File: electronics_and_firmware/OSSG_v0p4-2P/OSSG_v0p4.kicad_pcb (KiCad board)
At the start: 4 copper layers, 85 x 9 mm, 72 parts, among them J1 Conn_01x05_Male, J2 Ext RGB, J3 USB_B_Micro, J4 Touch, Q1 2SC4617R BR, Q2 2SC4617R BR, Q3 PMZ290UNE2YL, Q4 EMF20B02V, SW1 SW_SPST, SW2 Power, U1 MP23DB01HPTR, U2 ESP32-PICO-D4, U3 CH9102F, U4 XC61CC3002MR, U5 AP5054HTC, U6 MAX17048, U7 NCP167BMX330TBG, U8 SY7088

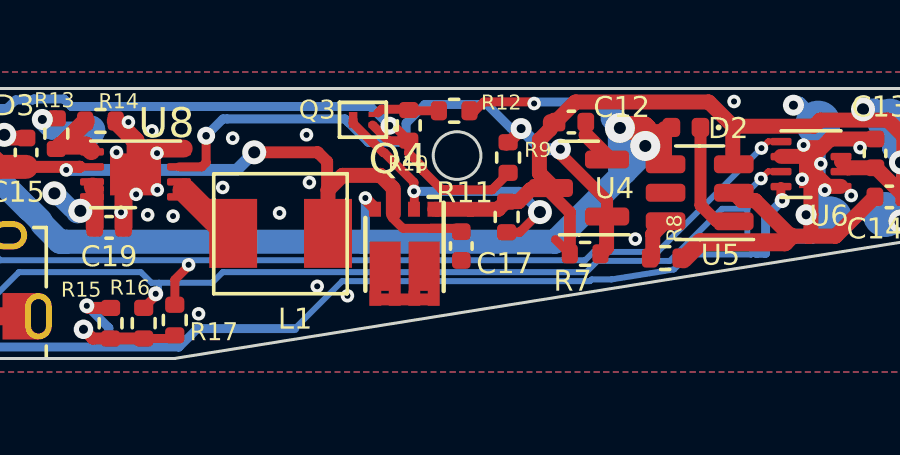
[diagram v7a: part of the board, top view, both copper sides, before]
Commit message: change Q4 footprint
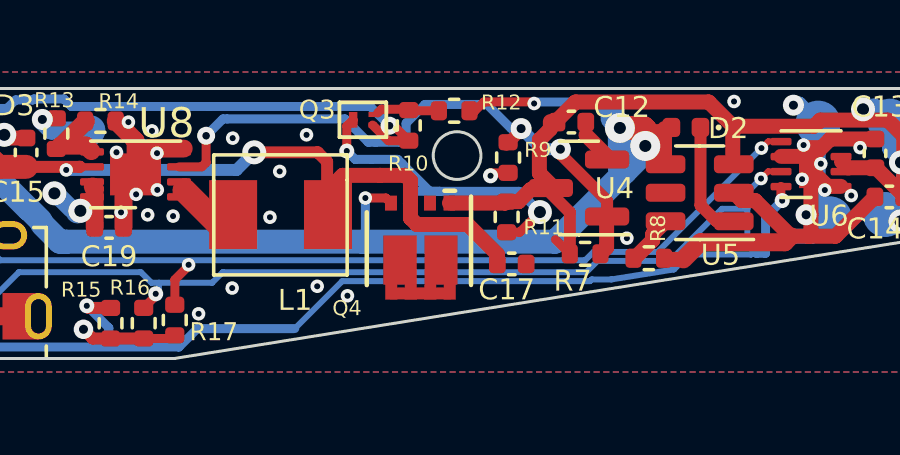
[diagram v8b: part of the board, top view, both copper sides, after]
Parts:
- C10, C11, C6: value 0.1uF -> 100nF
- C14: value 22uF/16V -> 22uF
- D1: value WS2812C-2020 -> WS2812B-2020
- Q4: value EMF20B02V -> YJQD30P02A; footprint OSSG_footprints:EMF20B02V -> OSSG_footprints:YJQD30P02A_DFN3.3x3.3
- R16: value 10k -> 10K
- R7: value 100k -> 100K
- moved C17 1.78 mm to (146.2, 80.8), turned to 0 degrees
- moved L1 0.63 mm to (138.5, 79.2)
- moved Q4 0.57 mm to (143.1, 80.2)
- moved R8 0.55 mm to (150.8, 80.7)
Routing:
- net Net-(C15-Pad1): track 22.1 -> 23.8 mm
- net Net-(Q3-Pad3): track 9.76 -> 10.8 mm
- net BATT1-: track 76.9 -> 77.6 mm
- net VBUS: track 63.0 -> 63.6 mm
- net BATT+: track 79.0 -> 78.4 mm
- net Net-(Q3-Pad1): track 35.6 -> 35.7 mm, vias 2 -> 3
